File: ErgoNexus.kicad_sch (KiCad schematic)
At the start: 110 parts, among them J7 Conn_01x02, J8 Conn_01x02, SW1 SW_Push, SW2 RotaryEncoder_Switch, SW3 SW_Push, SW4 RotaryEncoder_Switch, U1 SuperMini nRF52840, U2 SuperMini nRF52840

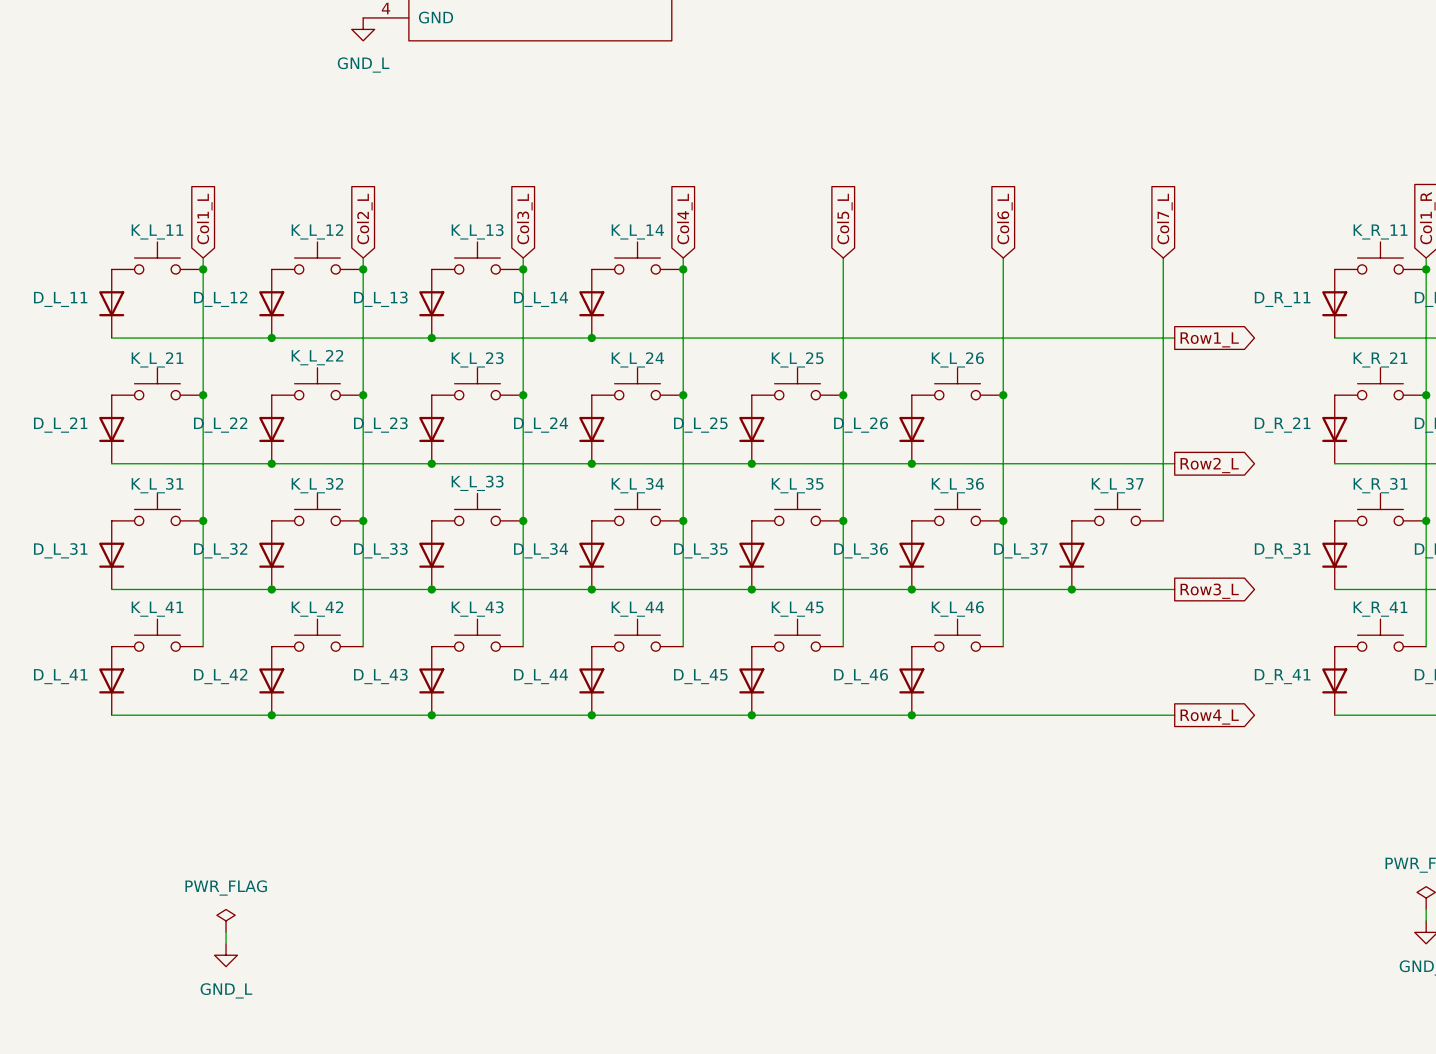
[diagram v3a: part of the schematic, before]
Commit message: feat: 左手の回路図の配置を修正
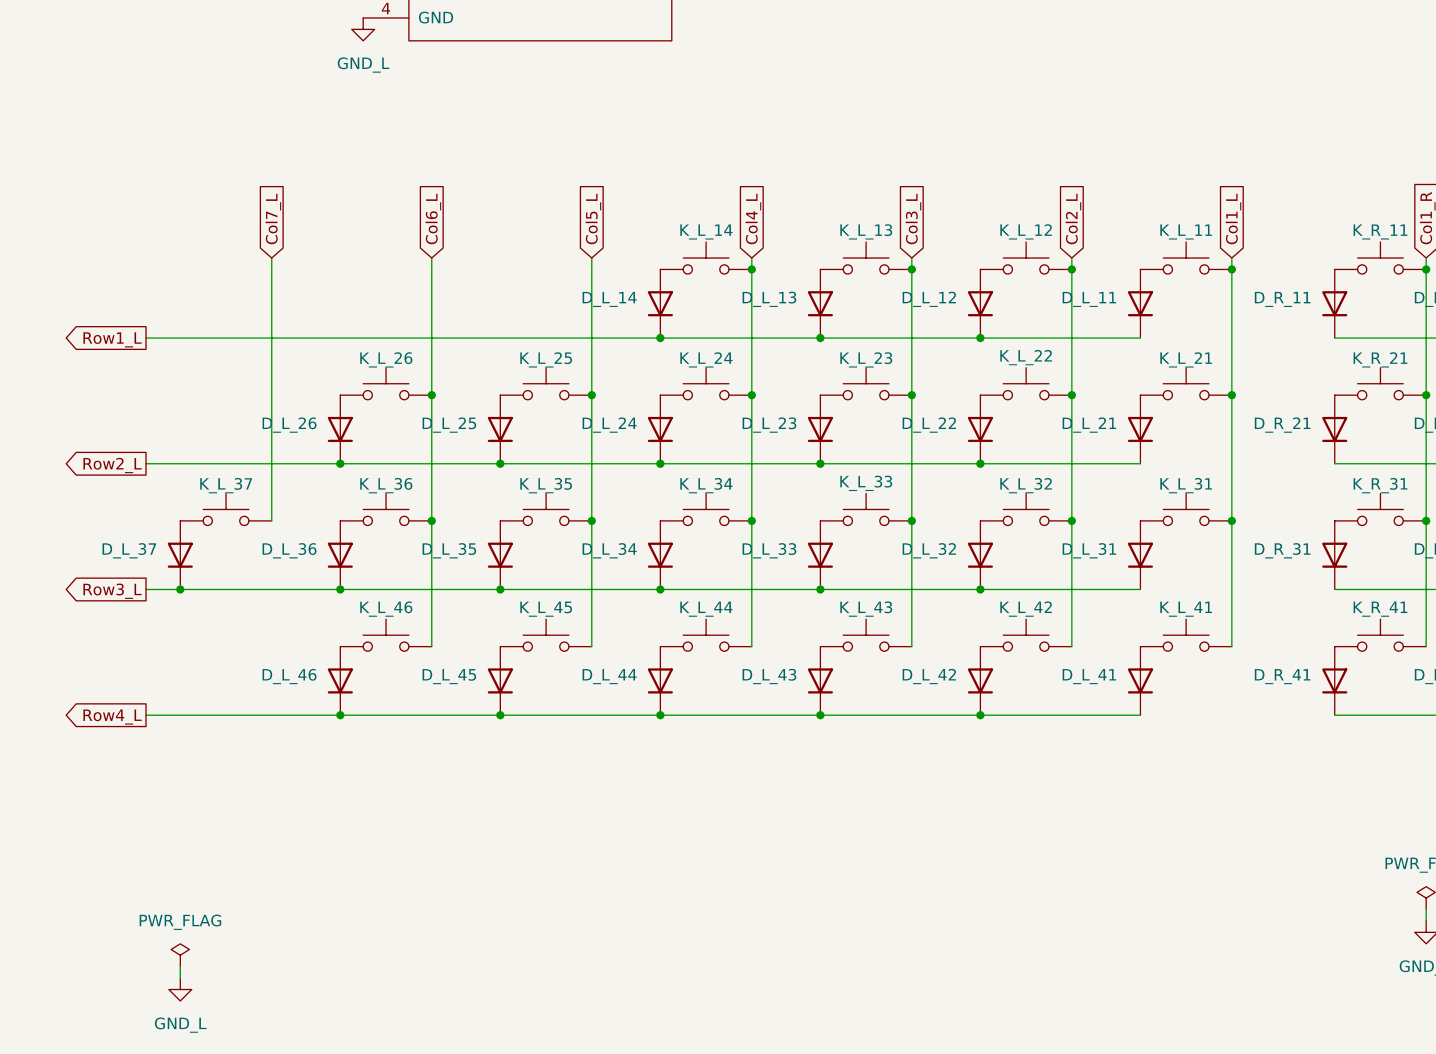
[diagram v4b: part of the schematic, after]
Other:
- moved on the sheet: D_L_11, D_L_12, D_L_13, D_L_14, D_L_21, D_L_22, D_L_23, D_L_24, D_L_25, D_L_26, D_L_31, D_L_32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

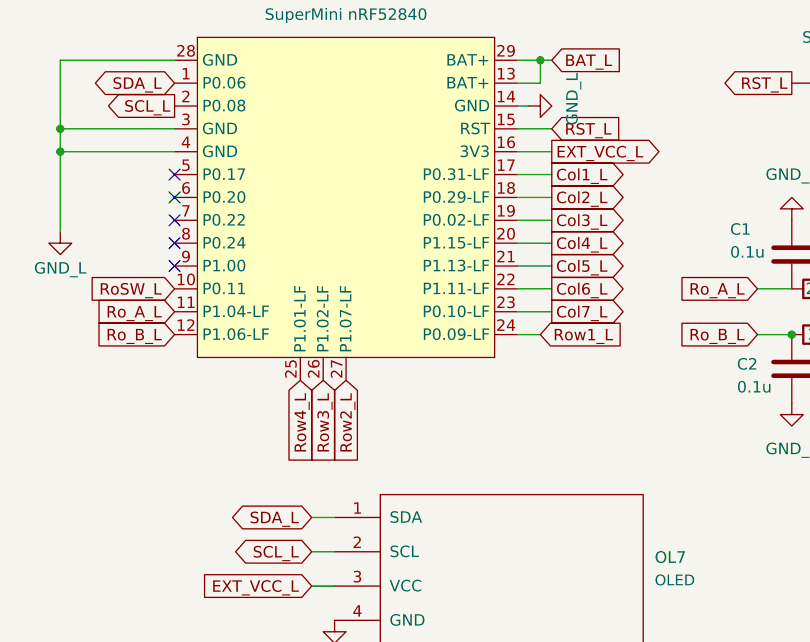
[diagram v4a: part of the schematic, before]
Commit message: feat: 左手の配線完了
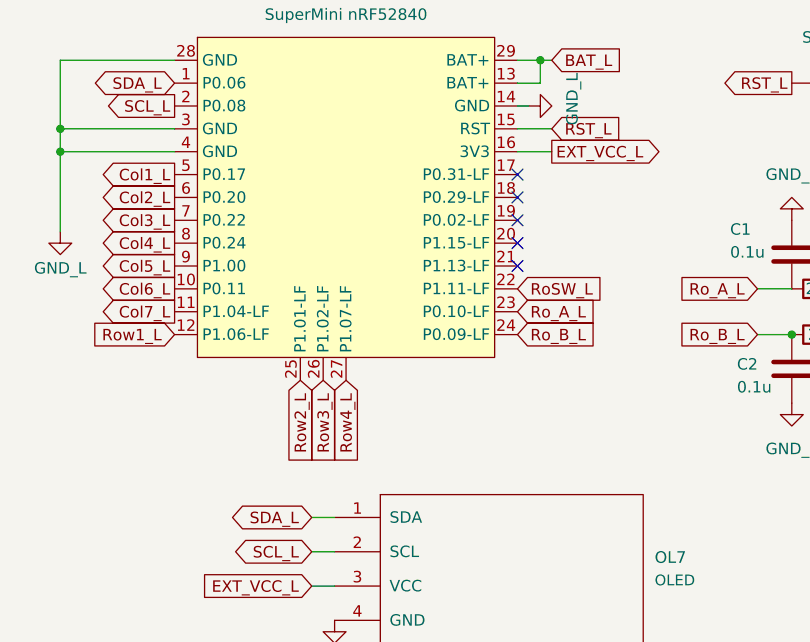
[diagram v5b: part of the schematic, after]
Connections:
- net Col1_L: now also U1.5 (P0.17); no longer U1.17 (P0.31-LF)
- net Col2_L: now also U1.6 (P0.20); no longer U1.18 (P0.29-LF)
- net Col3_L: now also U1.7 (P0.22); no longer U1.19 (P0.02-LF)
- net Col4_L: now also U1.8 (P0.24); no longer U1.20 (P1.15-LF)
- net Col5_L: now also U1.9 (P1.00); no longer U1.21 (P1.13-LF)
- net Col6_L: now also U1.10 (P0.11); no longer U1.22 (P1.11-LF)
- net Col7_L: now also U1.11 (P1.04-LF); no longer U1.23 (P0.10-LF)
- net RoSW_L: now also U1.22 (P1.11-LF); no longer U1.10 (P0.11)
- net Ro_A_L: now also U1.23 (P0.10-LF); no longer U1.11 (P1.04-LF)
- net Ro_B_L: now also U1.24 (P0.09-LF); no longer U1.12 (P1.06-LF)
- net Row1_L: now also U1.12 (P1.06-LF); no longer U1.24 (P0.09-LF)
- net Row2_L: now also U1.25 (P1.01-LF); no longer U1.27 (P1.07-LF)
- net Row4_L: now also U1.27 (P1.07-LF); no longer U1.25 (P1.01-LF)

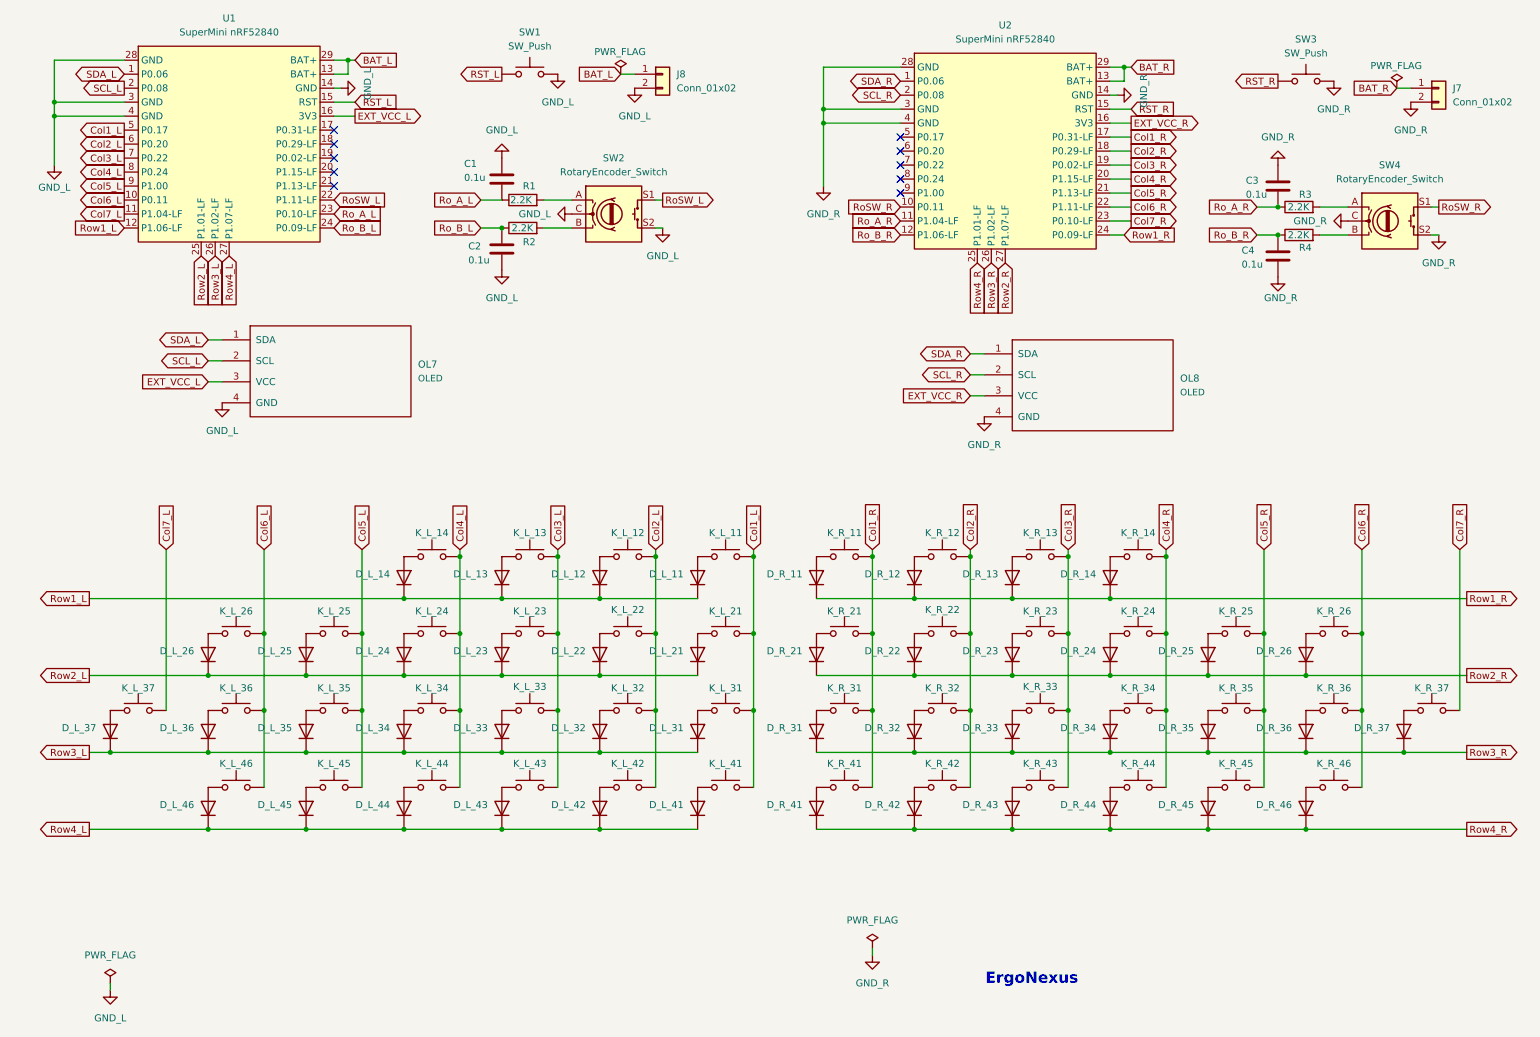
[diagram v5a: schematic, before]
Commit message: feat: remove one key and oled. little finger place update
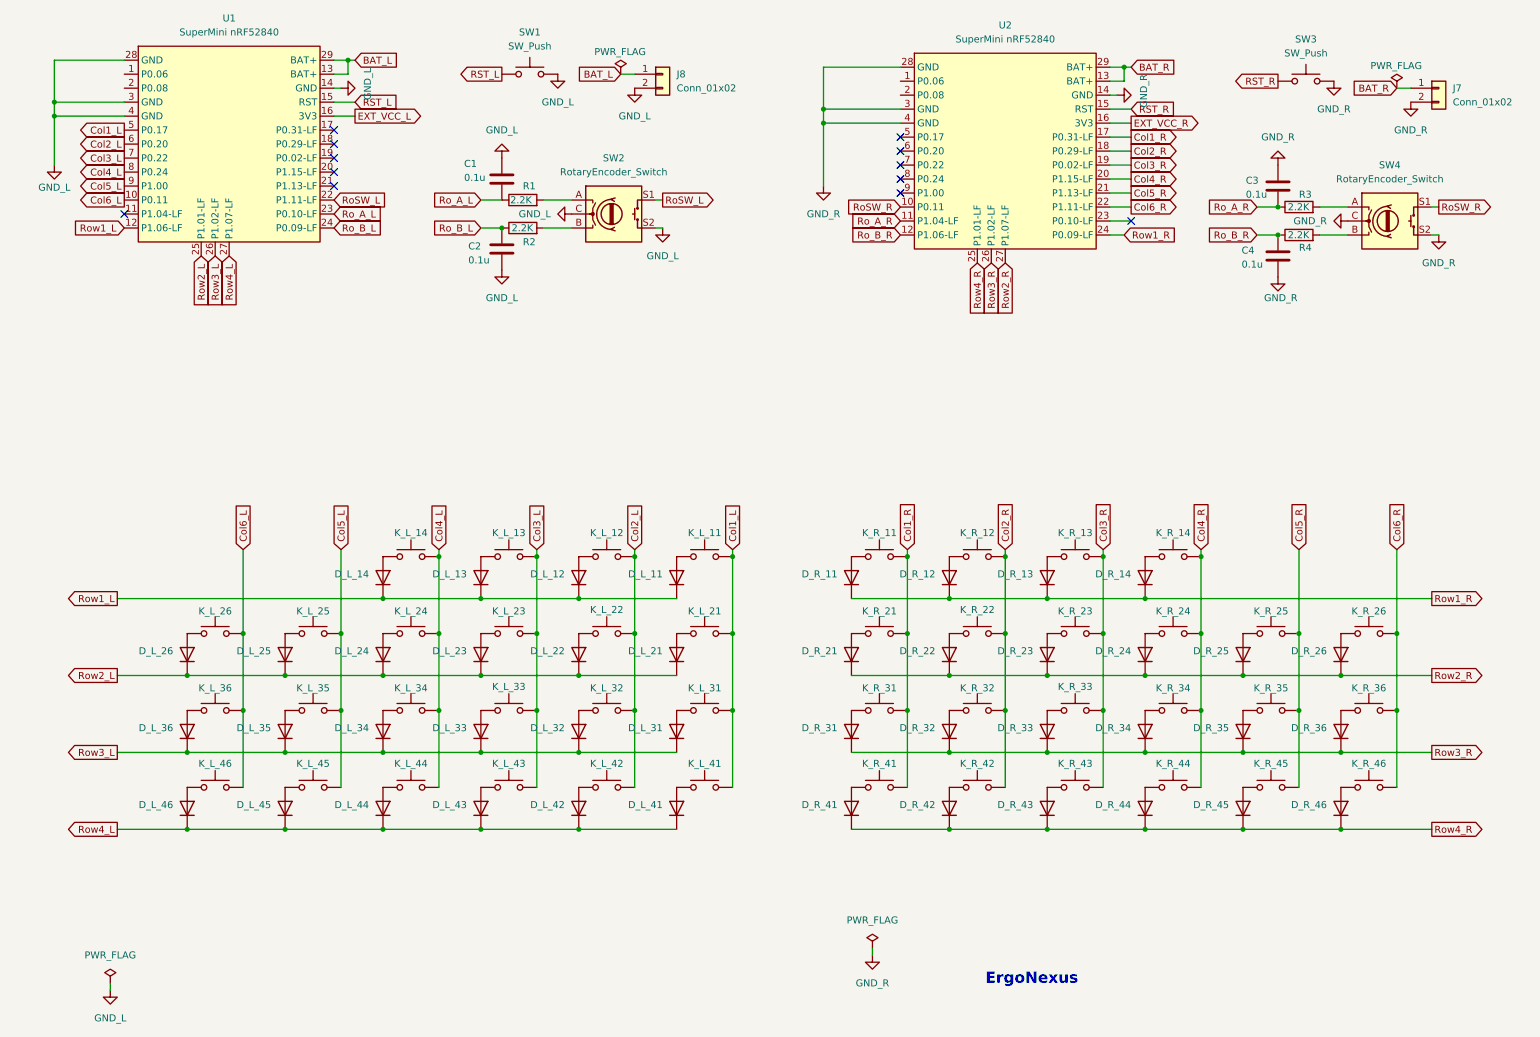
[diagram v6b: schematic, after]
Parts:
- removed D_L_37, D_R_37: 1N4148, kbd_Parts:Diode_TH_SMD, symbol Diode:1N4148
- removed K_L_37, K_R_37: SW_Push, kbd_SW:CherryMX_Hotswap_1u, symbol Switch:SW_Push
- removed OL7, OL8: OLED, kbd_Parts:OLED, symbol kbd:OLED
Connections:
- net Col7_L: no longer names the net of U1.11 (P1.04-LF)
- net Col7_R: no longer names the net of U2.23 (P0.10-LF)
- net SCL_L: no longer names the net of U1.2 (P0.08)
- net SCL_R: no longer names the net of U2.2 (P0.08)
- net SDA_L: no longer names the net of U1.1 (P0.06)
- net SDA_R: no longer names the net of U2.1 (P0.06)
- no-connect marks 10 -> 12
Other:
- moved on the sheet: D_L_11, D_L_12, D_L_13, D_L_14, D_L_21, D_L_22, D_L_23, D_L_24, D_L_25, D_L_26, D_L_31, D_L_32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
